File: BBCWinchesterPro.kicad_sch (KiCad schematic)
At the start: 31 parts, among them J1 Conn_02x17_Odd_Even, J2 Conn_01x04_Male, J3 Conn_01x02_Male, J4 Conn_02x20_Odd_Even, J5 Conn_02x20_Odd_Even, J6 Conn_02x20_Odd_Even, P1 CONN_01X02, P2 CONN_01x03, U1 74LS02, U2 74LS139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

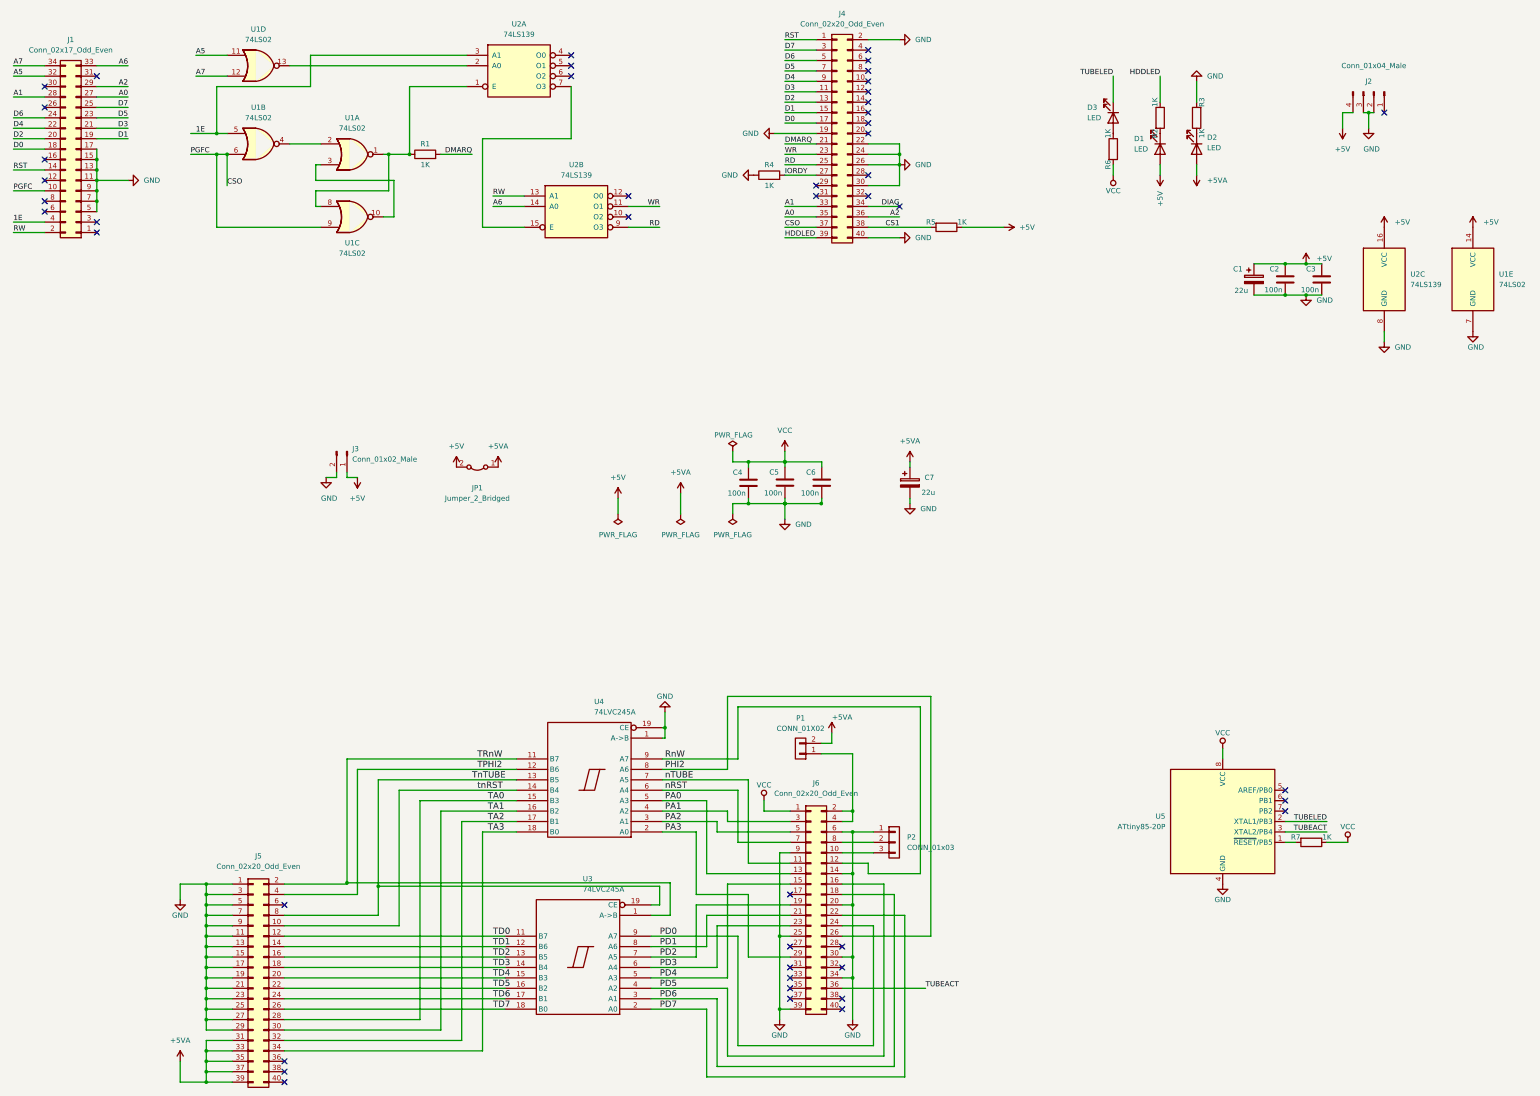
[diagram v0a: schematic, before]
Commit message: Annotate schematic and export as PDF
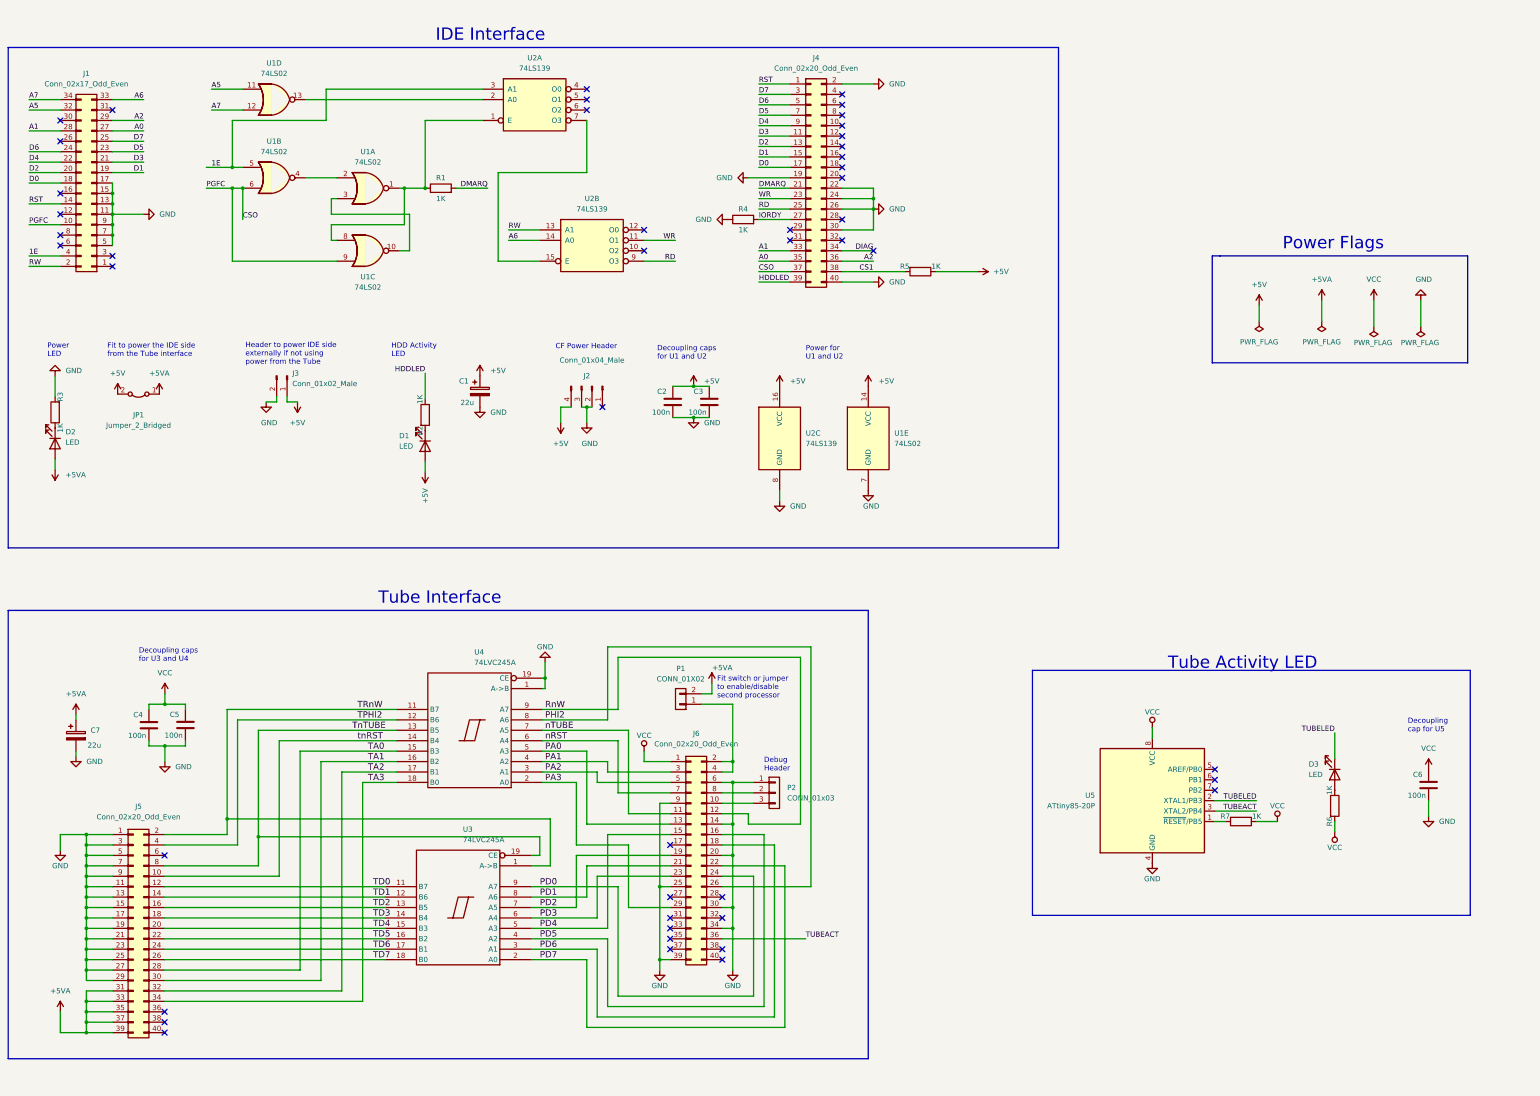
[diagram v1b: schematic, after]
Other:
- note added: "CF Power Header"
- note added: "Debug Header"
- note added: "Decoupling cap for U5"
- note added: "Decoupling caps for U1 and U2"
- note added: "Decoupling caps for U3 and U4"
- note added: "Fit switch or jumper to enable/disable second processor"
- note added: "Fit to power the IDE side from the Tube interface"
- note added: "HDD Activity LED"
- note added: "Header to power IDE side externally if not using power from the Tube"
- note added: "IDE Interface"
- note added: "Power Flags"
- note added: "Power LED"
- note added: "Power for U1 and U2"
- note added: "Tube Activity LED"
- note added: "Tube Interface"
- moved on the sheet: C1, C2, C3, C4, C5, C6, C7, D1, D2, D3, J1, J2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
